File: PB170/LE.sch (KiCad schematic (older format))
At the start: 7 parts

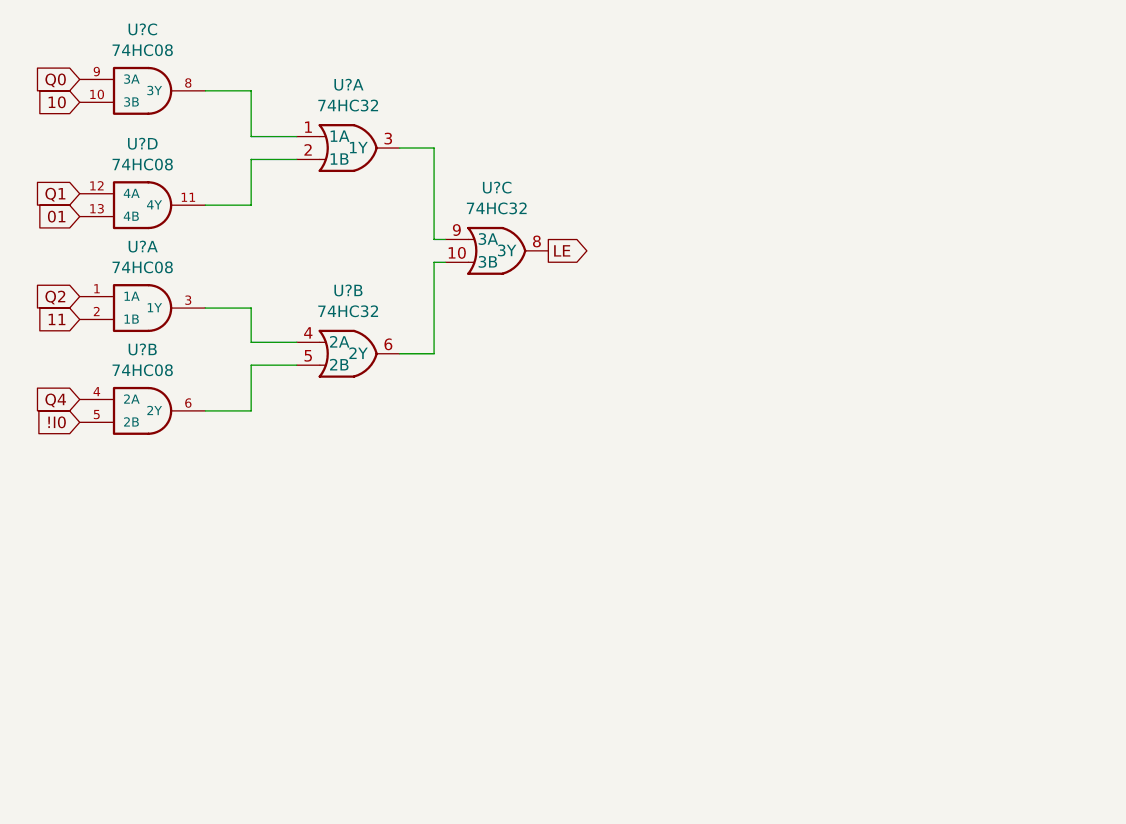
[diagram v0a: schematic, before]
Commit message: added LEDs, mby we could try to start routing
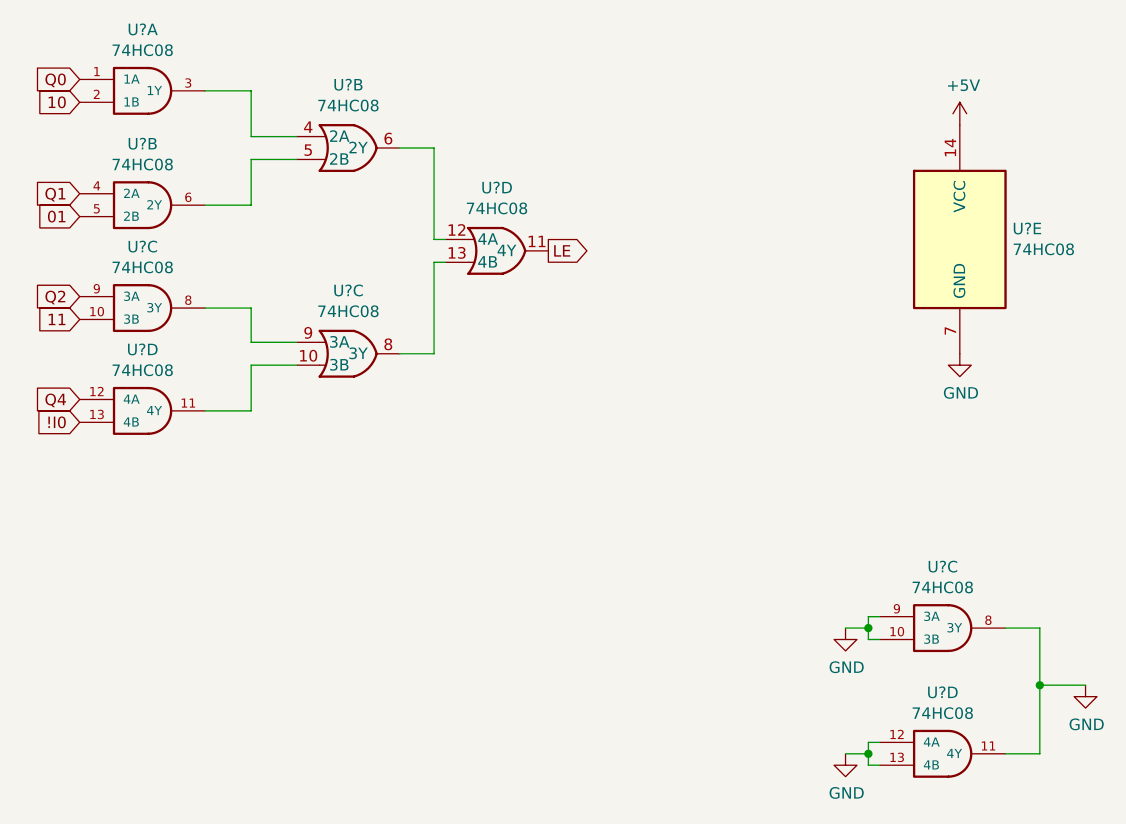
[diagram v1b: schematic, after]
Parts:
- added U? (x3): 74HC08, Housings_SOIC:SOIC-14_3.9x8.7mm_Pitch1.27mm, symbol PB170:74HC08
- U? (x3): value 74HC32 -> 74HC08
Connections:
- net !I0: now also U?.13 (4B); no longer U?.5 (2B)
- net 01: now also U?.5 (2B); no longer U?.13 (4B)
- net 10: now also U?.2 (1B); no longer U?.10 (3B)
- net 11: now also U?.10 (3B); no longer U?.2 (1B)
- net LE: now also U?.11 (4Y); no longer U?.8 (3Y)
- net Q0: now also U?.1 (1A); no longer U?.9 (3A)
- net Q1: now also U?.4 (2A); no longer U?.12 (4A)
- net Q2: now also U?.9 (3A); no longer U?.1 (1A)
- net Q4: now also U?.12 (4A); no longer U?.4 (2A)
- new net: U?.3 (1Y), U?.4 (2A)
- new net: U?.5 (2B), U?.6 (2Y)
- new net: U?.8 (3Y), U?.9 (3A)
- new net: U?.10 (3B), U?.11 (4Y)
- new net: U?.12 (4A), U?.6 (2Y)
- new net: U?.13 (4B), U?.8 (3Y)
- new net +5V: U?.14 (VCC)
- new net GND: U?.10 (3B), U?.11 (4Y), U?.12 (4A), U?.13 (4B), U?.7 (GND), U?.8 (3Y), U?.9 (3A)
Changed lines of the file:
@@
 $Comp
 L PB170:74HC08 U?
-U 3 1 602725DE
+U 1 1 602725DE
 P 5600 2850
 F 0 "U?" H 5625 3117 50  0000 C CNN
@@
 F 3 "https://datasheet.lcsc.com/szlcsc/Nexperia-74HC08D-653_C5593.pdf" H 5600 2850 50  0001 C CNN
 F 4 "C5593" H 5600 2850 50  0001 C CNN "LCSC"
-	3    5600 2850
-	1    0    0    -1
-$EndComp
-$Comp
-L PB170:74HC08 U?
-U 4 1 602728F1
+	1    5600 2850
+	1    0    0    -1
+$EndComp
+$Comp
+L PB170:74HC08 U?
+U 2 1 602728F1
 P 5600 3350
 F 0 "U?" H 5625 3617 50  0000 C CNN
@@
 F 3 "https://datasheet.lcsc.com/szlcsc/Nexperia-74HC08D-653_C5593.pdf" H 5600 3350 50  0001 C CNN
 F 4 "C5593" H 5600 3350 50  0001 C CNN "LCSC"
-	4    5600 3350
-	1    0    0    -1
-$EndComp
-$Comp
-L PB170:74HC08 U?
-U 1 1 60272E03
+	2    5600 3350
+	1    0    0    -1
+$EndComp
+$Comp
+L PB170:74HC08 U?
+U 3 1 60272E03
 P 5600 3800
 F 0 "U?" H 5625 4067 50  0000 C CNN
@@
 F 3 "https://datasheet.lcsc.com/szlcsc/Nexperia-74HC08D-653_C5593.pdf" H 5600 3800 50  0001 C CNN
 F 4 "C5593" H 5600 3800 50  0001 C CNN "LCSC"
-	1    5600 3800
-	1    0    0    -1
-$EndComp
-$Comp
-L PB170:74HC08 U?
-U 2 1 602733B4
+	3    5600 3800
+	1    0    0    -1
+$EndComp
+$Comp
+L PB170:74HC08 U?
+U 4 1 602733B4
 P 5600 4250
 F 0 "U?" H 5625 4517 50  0000 C CNN
@@
 F 3 "https://datasheet.lcsc.com/szlcsc/Nexperia-74HC08D-653_C5593.pdf" H 5600 4250 50  0001 C CNN
 F 4 "C5593" H 5600 4250 50  0001 C CNN "LCSC"
-	2    5600 4250
+	4    5600 4250
 	1    0    0    -1
 $EndComp
 $Comp
 L PB170:74HC32 U?
-U 1 1 60274388
+U 2 1 60274388
 P 6550 3100
 F 0 "U?" H 6525 3375 50  0000 C CNN
-F 1 "74HC32" H 6525 3284 50  0000 C CNN
+F 1 "74HC08" H 6525 3284 50  0000 C CNN
 F 2 "Housings_SOIC:SOIC-14_3.9x8.7mm_Pitch1.27mm" H 6000 3300 50  0001 C CNN
-F 3 "https://datasheet.lcsc.com/szlcsc/Nexperia-74HC32D-653_C5632.pdf" H 6000 3300 50  0001 C CNN
+F 3 "https://datasheet.lcsc.com/szlcsc/Nexperia-74HC08D-653_C5593.pdf" H 6000 3300 50  0001 C CNN
 F 4 "C5632" H 6550 3100 50  0001 C CNN "LCSC"
-	1    6550 3100
+	2    6550 3100
 	1    0    0    -1
 $EndComp
 $Comp
 L PB170:74HC32 U?
-U 2 1 60274C1B
+U 3 1 60274C1B
 P 6550 4000
 F 0 "U?" H 6525 4275 50  0000 C CNN
-F 1 "74HC32" H 6525 4184 50  0000 C CNN
+F 1 "74HC08" H 6525 4184 50  0000 C CNN
 F 2 "Housings_SOIC:SOIC-14_3.9x8.7mm_Pitch1.27mm" H 6000 4200 50  0001 C CNN
-F 3 "https://datasheet.lcsc.com/szlcsc/Nexperia-74HC32D-653_C5632.pdf" H 6000 4200 50  0001 C CNN
+F 3 "https://datasheet.lcsc.com/szlcsc/Nexperia-74HC08D-653_C5593.pdf" H 6000 4200 50  0001 C CNN
 F 4 "C5632" H 6550 4000 50  0001 C CNN "LCSC"
-	2    6550 4000
+	3    6550 4000
 	1    0    0    -1
 $EndComp
 $Comp
 L PB170:74HC32 U?
-U 3 1 602758C2
+U 4 1 602758C2
 P 7200 3550
 F 0 "U?" H 7175 3825 50  0000 C CNN
-F 1 "74HC32" H 7175 3734 50  0000 C CNN
+F 1 "74HC08" H 7175 3734 50  0000 C CNN
 F 2 "Housings_SOIC:SOIC-14_3.9x8.7mm_Pitch1.27mm" H 6650 3750 50  0001 C CNN
-F 3 "https://datasheet.lcsc.com/szlcsc/Nexperia-74HC32D-653_C5632.pdf" H 6650 3750 50  0001 C CNN
+F 3 "https://datasheet.lcsc.com/szlcsc/Nexperia-74HC08D-653_C5593.pdf" H 6650 3750 50  0001 C CNN
 F 4 "C5632" H 7200 3550 50  0001 C CNN "LCSC"
-	3    7200 3550
+	4    7200 3550
 	1    0    0    -1
 $EndComp
@@
 Text GLabel 5350 3850 0    50   Input ~ 0
 11
+$Comp
+L PB170:74HC08 U?
+U 5 1 60280504
+P 9200 3500
+AR Path="/6026D736/60280504" Ref="U?"  Part="5"
+AR Path="/60271299/60280504" Ref="U?"  Part="5"
+F 0 "U?" H 9430 3546 50  0000 L CNN
+F 1 "74HC08" H 9430 3455 50  0000 L CNN
+F 2 "Housings_SOIC:SOIC-14_3.9x8.7mm_Pitch1.27mm" H 9200 3500 50  0001 C CNN
+F 3 "https://datasheet.lcsc.com/szlcsc/Nexperia-74HC08D-653_C5593.pdf" H 9200 3500 50  0001 C CNN
+F 4 "C5593" H 9200 3500 50  0001 C CNN "LCSC"
+	5    9200 3500
+	1    0    0    -1
+$EndComp
+$Comp
+L power:GND #PWR?
+U 1 1 6028050A
+P 9200 4000
+AR Path="/6026D736/6028050A" Ref="#PWR?"  Part="1"
+AR Path="/60271299/6028050A" Ref="#PWR?"  Part="1"
+F 0 "#PWR?" H 9200 3750 50  0001 C CNN
+F 1 "GND" H 9205 3827 50  0000 C CNN
+F 2 "" H 9200 4000 50  0001 C CNN
+F 3 "" H 9200 4000 50  0001 C CNN
+	1    9200 4000
+	1    0    0    -1
+$EndComp
+$Comp
+L power:+5V #PWR?
+U 1 1 60280510
+P 9200 3000
+AR Path="/6026D736/60280510" Ref="#PWR?"  Part="1"
+AR Path="/60271299/60280510" Ref="#PWR?"  Part="1"
+F 0 "#PWR?" H 9200 2850 50  0001 C CNN
+F 1 "+5V" H 9215 3173 50  0000 C CNN
+F 2 "" H 9200 3000 50  0001 C CNN
+F 3 "" H 9200 3000 50  0001 C CNN
+	1    9200 3000
+	1    0    0    -1
+$EndComp
+$Comp
+L PB170:74HC08 U?
+U 3 1 60289CEE
+P 9100 5200
+F 0 "U?" H 9125 5467 50  0000 C CNN
+F 1 "74HC08" H 9125 5376 50  0000 C CNN
+F 2 "Housings_SOIC:SOIC-14_3.9x8.7mm_Pitch1.27mm" H 9100 5200 50  0001 C CNN
+F 3 "https://datasheet.lcsc.com/szlcsc/Nexperia-74HC08D-653_C5593.pdf" H 9100 5200 50  0001 C CNN
+F 4 "C5593" H 9100 5200 50  0001 C CNN "LCSC"
+	3    9100 5200
+	1    0    0    -1
+$EndComp
+$Comp
+L power:GND #PWR?
+U 1 1 6028B97C
+P 9750 5450
+F 0 "#PWR?" H 9750 5200 50  0001 C CNN
+F 1 "GND" H 9755 5277 50  0000 C CNN
+F 2 "" H 9750 5450 50  0001 C CNN
+F 3 "" H 9750 5450 50  0001 C CNN
+	1    9750 5450
+	1    0    0    -1
+$EndComp
+Wire Wire Line
+	9400 5200 9550 5200
+Wire Wire Line
+	9550 5450 9750 5450
+Wire Wire Line
+	9400 5750 9550 5750
+Wire Wire Line
+	9550 5200 9550 5450
+Connection ~ 9550 5450
+Wire Wire Line
+	9550 5450 9550 5750
+$Comp
+L power:GND #PWR?
+U 1 1 6028CD52
+P 8700 5200
+F 0 "#PWR?" H 8700 4950 50  0001 C CNN
+F 1 "GND" H 8705 5027 50  0000 C CNN
+F 2 "" H 8700 5200 50  0001 C CNN
+F 3 "" H 8700 5200 50  0001 C CNN
+	1    8700 5200
+	1    0    0    -1
+$EndComp
+Wire Wire Line
+	8850 5150 8800 5150
+Wire Wire Line
+	8800 5150 8800 5200
+Wire Wire Line
+	8800 5200 8700 5200
+Wire Wire Line
+	8800 5200 8800 5250
+Wire Wire Line
+	8800 5250 8850 5250
+Connection ~ 8800 5200
+$Comp
+L PB170:74HC08 U?
+U 4 1 6028F1C4
+P 9100 5750
+F 0 "U?" H 9125 6017 50  0000 C CNN
+F 1 "74HC08" H 9125 5926 50  0000 C CNN
+F 2 "Housings_SOIC:SOIC-14_3.9x8.7mm_Pitch1.27mm" H 9100 5750 50  0001 C CNN
+F 3 "https://datasheet.lcsc.com/szlcsc/Nexperia-74HC08D-653_C5593.pdf" H 9100 5750 50  0001 C CNN
+F 4 "C5593" H 9100 5750 50  0001 C CNN "LCSC"
+	4    9100 5750
+	1    0    0    -1
+$EndComp
+$Comp
+L power:GND #PWR?
+U 1 1 6028F1CA
+P 8700 5750
+F 0 "#PWR?" H 8700 5500 50  0001 C CNN
+F 1 "GND" H 8705 5577 50  0000 C CNN
+F 2 "" H 8700 5750 50  0001 C CNN
+F 3 "" H 8700 5750 50  0001 C CNN
+	1    8700 5750
+	1    0    0    -1
+$EndComp
+Wire Wire Line
+	8850 5700 8800 5700
+Wire Wire Line
+	8800 5700 8800 5750
+Wire Wire Line
+	8800 5750 8700 5750
+Wire Wire Line
+	8800 5750 8800 5800
+Wire Wire Line
+	8800 5800 8850 5800
+Connection ~ 8800 5750
 $EndSCHEMATC
